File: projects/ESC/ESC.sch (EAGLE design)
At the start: 92 parts, among them J1 1755529, J2 1755529, J3 1755529, J4 1755529, U1 STM32F405RGT6, U10 CSD88584Q5DCT, U11 CSD88584Q5DCT, U12 CSD88584Q5DCT, U13 CSD88584Q5DCT, U2 CSD88584Q5DCT, U3 CSD88584Q5DCT, U4 CSD88584Q5DCT, U5 CSD88584Q5DCT, U6 CSD88584Q5DCT, U7 CSD88584Q5DCT, U8 CSD88584Q5DCT, U9 CSD88584Q5DCT, Y1 ECS-80-S-4X

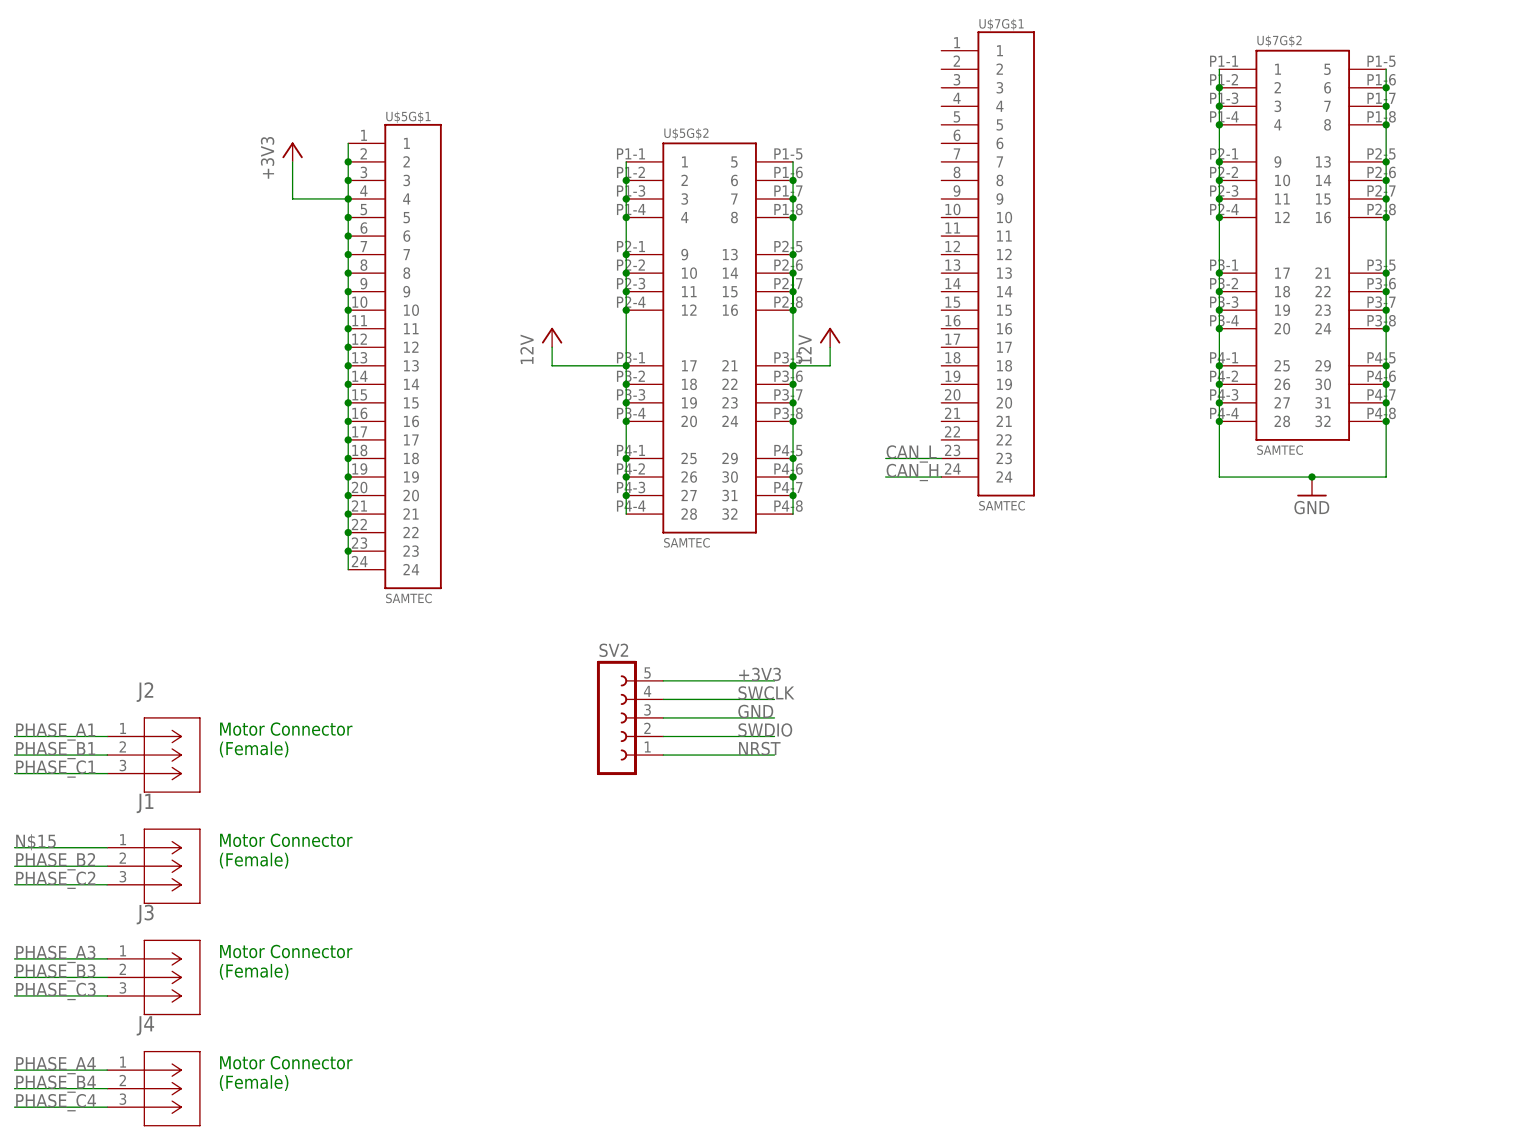
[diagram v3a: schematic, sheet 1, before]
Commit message: made wires thicker
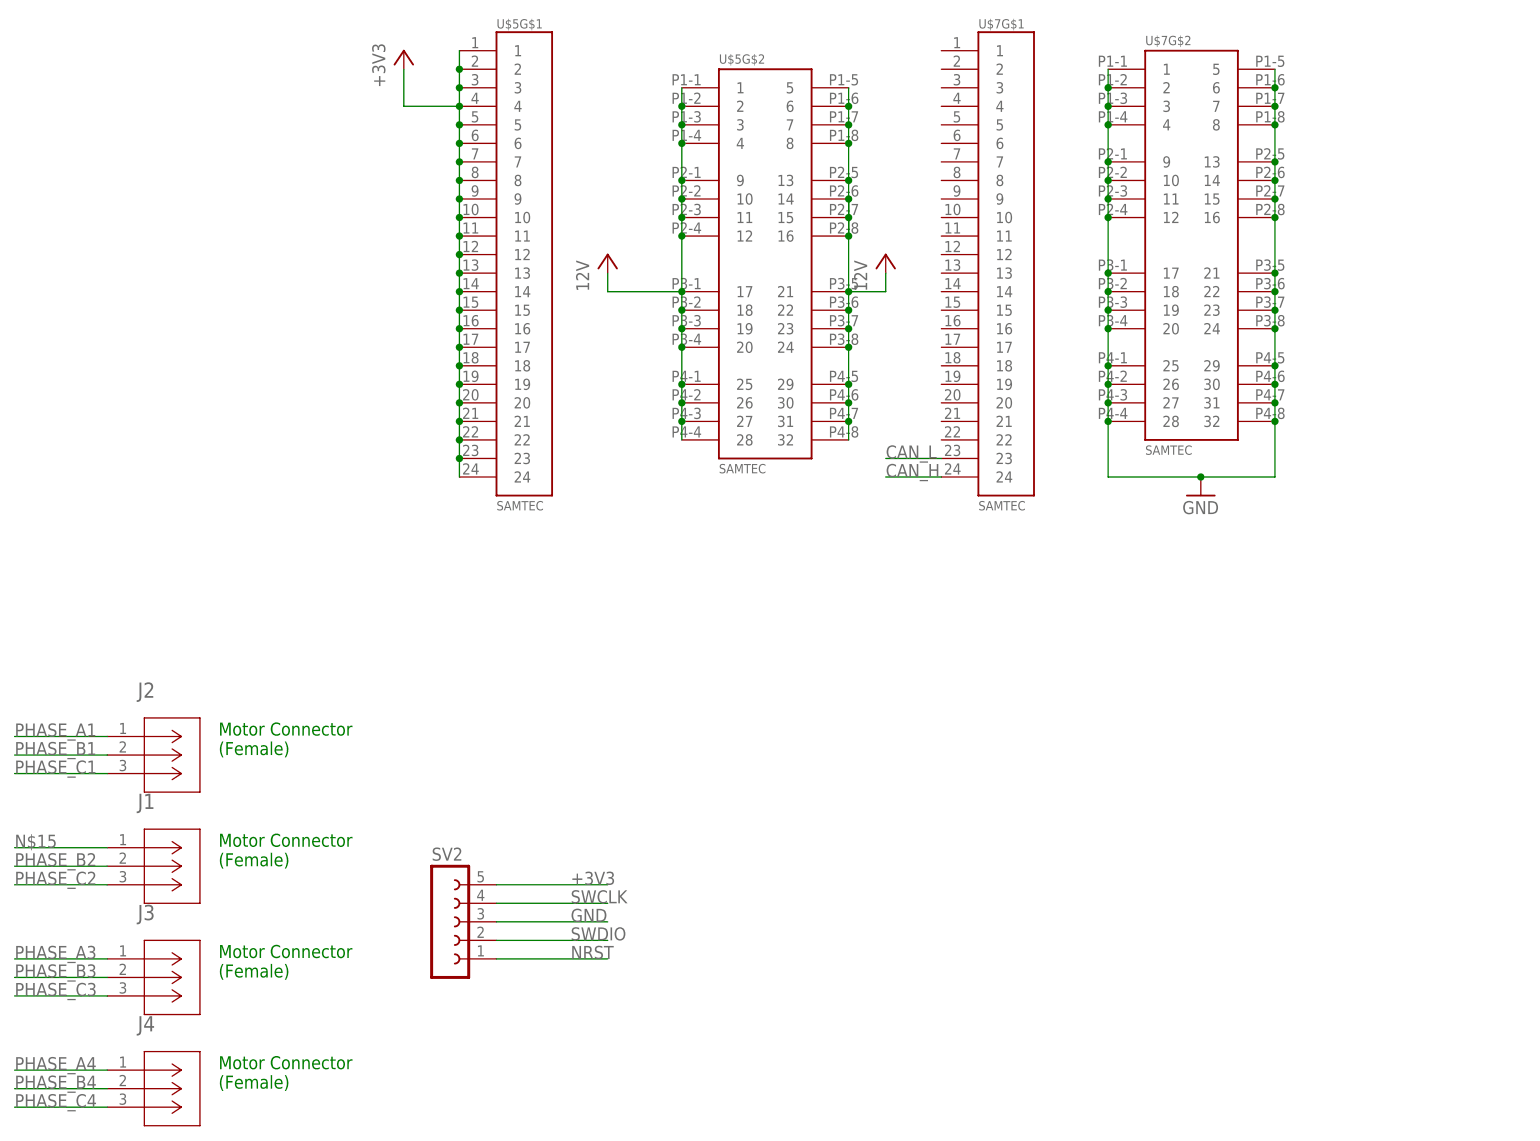
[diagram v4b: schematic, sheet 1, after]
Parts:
- removed SV1: (no value), con-lsta:FE05-1
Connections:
- new net DVDD_2: C23.1, R19.2, R21.2, U$1G$2.DVDD
- net +3V3: no longer SV1.5
- net 12V: no longer C23.1, R10.2, R19.2, R21.2, R8.2, U$1G$2.DVDD
- net DVDD_1: now also R10.2, R8.2
- net GND: no longer SV1.3
- net NRST: no longer SV1.1
- net SWCLK: no longer SV1.4
- net SWDIO: no longer SV1.2
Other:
- moved on the sheet: C10, C12, C16, C32, C33, C34, C35, C38, C39, C4, C40, C41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

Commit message: starting motor 1 (finished motor 2)
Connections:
- net N$15 renamed PHASE_A2
- new net SLC_1B: U4.PGND, U4.PGND_2, U4.PGND_3, U4.PGND_4, U4.PGND_5, U4.PGND_6, U4.PGND_7, U4.PGND_8, U4.PGND_9
- net GHB_1: now also U4.GH; no longer U2.GH
- net GHC_1: now also U2.GH; no longer U4.GH
- net GLB_1: now also U4.GL; no longer U2.GL
- net GLC_1: now also U2.GL; no longer U4.GL
- net PHASE_B1: now also U4.VSW, U4.VSW_2, U4.VSW_3, U4.VSW_4, U4.VSW_5, U4.VSW_6, U4.VSW_7, U4.VSW_8, U4.VSW_9; no longer U2.VSW, U2.VSW_2, U2.VSW_3, U2.VSW_4, U2.VSW_5, U2.VSW_6, U2.VSW_7, U2.VSW_8, U2.VSW_9
- net PHASE_C1: now also U2.VSW, U2.VSW_2, U2.VSW_3, U2.VSW_4, U2.VSW_5, U2.VSW_6, U2.VSW_7, U2.VSW_8, U2.VSW_9; no longer U4.VSW, U4.VSW_2, U4.VSW_3, U4.VSW_4, U4.VSW_5, U4.VSW_6, U4.VSW_7, U4.VSW_8, U4.VSW_9
- net SHB_1: now also U4.SH; no longer U2.SH
- net SHC_1: now also U2.SH; no longer U4.SH
- net SLB_1: no longer U2.PGND, U2.PGND_2, U2.PGND_3, U2.PGND_4, U2.PGND_5, U2.PGND_6, U2.PGND_7, U2.PGND_8, U2.PGND_9
- net SLC_1: now also U2.PGND, U2.PGND_2, U2.PGND_3, U2.PGND_4, U2.PGND_5, U2.PGND_6, U2.PGND_7, U2.PGND_8, U2.PGND_9; no longer U4.PGND, U4.PGND_2, U4.PGND_3, U4.PGND_4, U4.PGND_5, U4.PGND_6, U4.PGND_7, U4.PGND_8, U4.PGND_9
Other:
- moved on the sheet: U2, U4, U5, U7

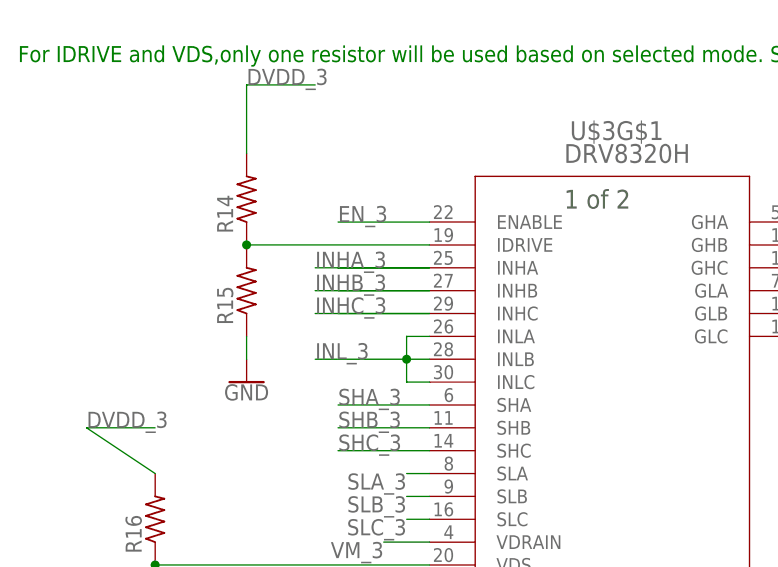
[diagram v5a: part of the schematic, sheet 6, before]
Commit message: finished the left half of the board
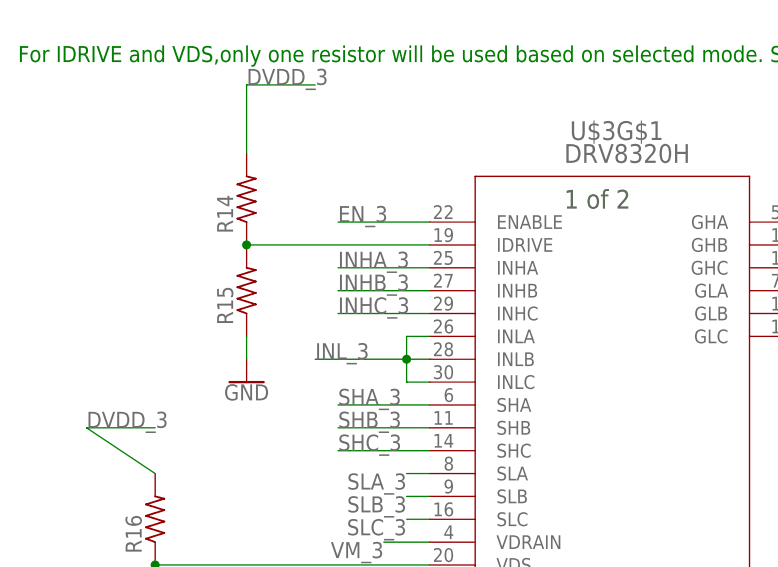
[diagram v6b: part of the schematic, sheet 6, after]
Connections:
- removed net N$10: U$2G$1.INHA
- removed net N$11: U$2G$1.INHB
- removed net N$14: U$2G$1.INHC
- removed net N$20: U$3G$1.INHA
- removed net N$21: U$3G$1.INHB
- removed net N$22: U$3G$1.INHC
- net INHA_1: now also U$2G$1.INHA
- net INHA_3: now also U$3G$1.INHA
- net INHB_1: now also U$2G$1.INHB
- net INHB_3: now also U$3G$1.INHB
- net INHC_1: now also U$2G$1.INHC
- net INHC_3: now also U$3G$1.INHC
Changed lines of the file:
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@@
-</segment>
-</net>
-<net name="N$10" class="0">
-<segment>
-<pinref part="U$2" gate="G$1" pin="INHA"/>
-<wire x1="-68.58" y1="25.4" x2="-78.74" y2="25.4" width="0.1524" layer="91"/>
-</segment>
-</net>
-<net name="N$11" class="0">
-<segment>
-<pinref part="U$2" gate="G$1" pin="INHB"/>
-<wire x1="-68.58" y1="22.86" x2="-78.74" y2="22.86" width="0.1524" layer="91"/>
-</segment>
-</net>
-<net name="N$14" class="0">
-<segment>
-<pinref part="U$2" gate="G$1" pin="INHC"/>
-<wire x1="-68.58" y1="20.32" x2="-78.74" y2="20.32" width="0.1524" layer="91"/>
 </segment>
 </net>
@@
 <net name="INHA_1" class="0">
 <segment>
-<wire x1="-68.58" y1="25.4" x2="-78.74" y2="25.4" width="0.1524" layer="91"/>
-<wire x1="-81.28" y1="25.4" x2="-78.74" y2="25.4" width="0.1524" layer="91"/>
 <label x="-81.28" y="25.4" size="1.778" layer="95"/>
+<pinref part="U$2" gate="G$1" pin="INHA"/>
+<wire x1="-81.28" y1="25.4" x2="-68.58" y2="25.4" width="0.1524" layer="91"/>
 </segment>
 </net>
 <net name="INHB_1" class="0">
 <segment>
-<wire x1="-68.58" y1="22.86" x2="-76.2" y2="22.86" width="0.1524" layer="91"/>
-<wire x1="-81.28" y1="22.86" x2="-76.2" y2="22.86" width="0.1524" layer="91"/>
 <label x="-81.28" y="22.86" size="1.778" layer="95"/>
-</segment>
-</net>
-<net name="INHC_1" class="0">
-<segment>
-<wire x1="-68.58" y1="20.32" x2="-78.74" y2="20.32" width="0.1524" layer="91"/>
-<wire x1="-81.28" y1="20.32" x2="-78.74" y2="20.32" width="0.1524" layer="91"/>
-<label x="-81.28" y="20.32" size="1.778" layer="95"/>
+<pinref part="U$2" gate="G$1" pin="INHB"/>
+<wire x1="-68.58" y1="22.86" x2="-81.28" y2="22.86" width="0.1524" layer="91"/>
 </segment>
 </net>
@@
 <wire x1="-68.58" y1="-7.62" x2="-99.06" y2="-7.62" width="0.1524" layer="91"/>
 <junction x="-99.06" y="-7.62"/>
+</segment>
+</net>
+<net name="INHC_1" class="0">
+<segment>
+<pinref part="U$2" gate="G$1" pin="INHC"/>
+<wire x1="-68.58" y1="20.32" x2="-81.28" y2="20.32" width="0.1524" layer="91"/>
+<label x="-81.28" y="20.32" size="1.778" layer="95"/>
 </segment>
 </net>
@@
 </busses>
 <nets>
-<net name="N$20" class="0">
-<segment>
-<pinref part="U$3" gate="G$1" pin="INHA"/>
-<wire x1="-58.42" y1="17.78" x2="-68.58" y2="17.78" width="0.1524" layer="91"/>
-</segment>
-</net>
-<net name="N$21" class="0">
-<segment>
-<pinref part="U$3" gate="G$1" pin="INHB"/>
-<wire x1="-58.42" y1="15.24" x2="-68.58" y2="15.24" width="0.1524" layer="91"/>
-</segment>
-</net>
-<net name="N$22" class="0">
-<segment>
-<pinref part="U$3" gate="G$1" pin="INHC"/>
-<wire x1="-58.42" y1="12.7" x2="-68.58" y2="12.7" width="0.1524" layer="91"/>
-</segment>
-</net>
 <net name="DVDD_3" class="0">
 <segment>
@@
 </segment>
 </net>
-<net name="INHA_3" class="0">
-<segment>
-<wire x1="-58.42" y1="17.78" x2="-68.58" y2="17.78" width="0.1524" layer="91"/>
-<wire x1="-71.12" y1="17.78" x2="-68.58" y2="17.78" width="0.1524" layer="91"/>
-<label x="-71.12" y="17.78" size="1.778" layer="95"/>
-</segment>
-</net>
-<net name="INHB_3" class="0">
-<segment>
-<wire x1="-58.42" y1="15.24" x2="-66.04" y2="15.24" width="0.1524" layer="91"/>
-<wire x1="-71.12" y1="15.24" x2="-66.04" y2="15.24" width="0.1524" layer="91"/>
-<label x="-71.12" y="15.24" size="1.778" layer="95"/>
-</segment>
-</net>
-<net name="INHC_3" class="0">
-<segment>
-<wire x1="-58.42" y1="12.7" x2="-68.58" y2="12.7" width="0.1524" layer="91"/>
-<wire x1="-71.12" y1="12.7" x2="-68.58" y2="12.7" width="0.1524" layer="91"/>
-<label x="-71.12" y="12.7" size="1.778" layer="95"/>
-</segment>
-</net>
 <net name="INL_3" class="0">
 <segment>
@@
 </segment>
 </net>
+<net name="INHA_3" class="0">
+<segment>
+<pinref part="U$3" gate="G$1" pin="INHA"/>
+<wire x1="-58.42" y1="17.78" x2="-68.58" y2="17.78" width="0.1524" layer="91"/>
+<label x="-68.58" y="17.78" size="1.778" layer="95"/>
+</segment>
+</net>
+<net name="INHB_3" class="0">
+<segment>
+<pinref part="U$3" gate="G$1" pin="INHB"/>
+<wire x1="-58.42" y1="15.24" x2="-68.58" y2="15.24" width="0.1524" layer="91"/>
+<label x="-68.58" y="15.24" size="1.778" layer="95"/>
+</segment>
+</net>
+<net name="INHC_3" class="0">
+<segment>
+<pinref part="U$3" gate="G$1" pin="INHC"/>
+<wire x1="-58.42" y1="12.7" x2="-68.58" y2="12.7" width="0.1524" layer="91"/>
+<label x="-68.58" y="12.7" size="1.778" layer="95"/>
+</segment>
+</net>

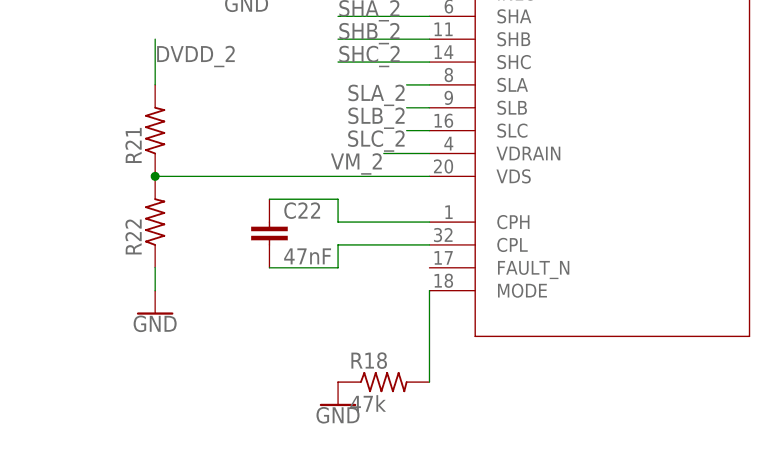
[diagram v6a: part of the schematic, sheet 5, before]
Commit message: Added Fault connection from drvs to stm
forgot to do this earlier
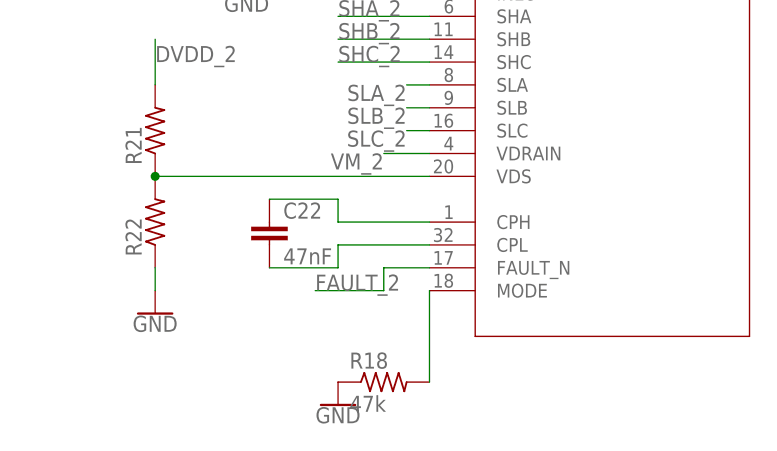
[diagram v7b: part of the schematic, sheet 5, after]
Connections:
- net FAULT_1: now also U$2G$1.FAULT_N
- net FAULT_2: now also U$1G$1.FAULT_N
- net FAULT_3: now also U$3G$1.FAULT_N
- net FAULT_4: now also U$4G$1.FAULT_N
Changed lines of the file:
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@@
 <?xml version="1.0" encoding="utf-8"?>
 <!DOCTYPE eagle SYSTEM "eagle.dtd">
-<eagle version="9.4.1">
+<eagle version="9.5.1">
 <drawing>
 <settings>
@@
 </segment>
 </net>
+<net name="FAULT_1" class="0">
+<segment>
+<pinref part="U$2" gate="G$1" pin="FAULT_N"/>
+<wire x1="-68.58" y1="-17.78" x2="-76.2" y2="-17.78" width="0.1524" layer="91"/>
+<label x="-76.2" y="-17.78" size="1.778" layer="95"/>
+</segment>
+</net>
 </nets>
 </sheet>
@@
 </segment>
 </net>
+<net name="FAULT_2" class="0">
+<segment>
+<pinref part="U$1" gate="G$1" pin="FAULT_N"/>
+<wire x1="71.12" y1="60.96" x2="66.04" y2="60.96" width="0.1524" layer="91"/>
+<wire x1="66.04" y1="60.96" x2="66.04" y2="58.42" width="0.1524" layer="91"/>
+<wire x1="66.04" y1="58.42" x2="58.42" y2="58.42" width="0.1524" layer="91"/>
+<label x="58.42" y="58.42" size="1.778" layer="95"/>
+</segment>
+</net>
 </nets>
 </sheet>
@@
 </segment>
 </net>
+<net name="FAULT_3" class="0">
+<segment>
+<pinref part="U$3" gate="G$1" pin="FAULT_N"/>
+<wire x1="-58.42" y1="-25.4" x2="-63.5" y2="-25.4" width="0.1524" layer="91"/>
+<wire x1="-63.5" y1="-25.4" x2="-63.5" y2="-27.94" width="0.1524" layer="91"/>
+<wire x1="-63.5" y1="-27.94" x2="-71.12" y2="-27.94" width="0.1524" layer="91"/>
+<label x="-71.12" y="-27.94" size="1.778" layer="95"/>
+</segment>
+</net>
 </nets>
 </sheet>
@@
 </segment>
 </net>
+<net name="FAULT_4" class="0">
+<segment>
+<pinref part="U$4" gate="G$1" pin="FAULT_N"/>
+<wire x1="-58.42" y1="-25.4" x2="-63.5" y2="-25.4" width="0.1524" layer="91"/>
+<wire x1="-63.5" y1="-25.4" x2="-63.5" y2="-27.94" width="0.1524" layer="91"/>
+<wire x1="-63.5" y1="-27.94" x2="-71.12" y2="-27.94" width="0.1524" layer="91"/>
+<label x="-71.12" y="-27.94" size="1.778" layer="95"/>
+</segment>
+</net>

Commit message: ERC stuff 1
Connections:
- removed net N$37: U$4G$1.INHA
- removed net N$38: U$4G$1.INHB
- removed net N$39: U$4G$1.INHC
- removed net SLC_1B: U4.PGND, U4.PGND_2, U4.PGND_3, U4.PGND_4, U4.PGND_5, U4.PGND_6, U4.PGND_7, U4.PGND_8, U4.PGND_9
- net INHA_4: now also U$4G$1.INHA
- net INHB_4: now also U$4G$1.INHB
- net INHC_2: now also U$1G$1.INHC
- net INHC_3: no longer U$1G$1.INHC
- net INHC_4: now also U$4G$1.INHC
- net SLB_1: now also U4.PGND, U4.PGND_2, U4.PGND_3, U4.PGND_4, U4.PGND_5, U4.PGND_6, U4.PGND_7, U4.PGND_8, U4.PGND_9
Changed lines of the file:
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@@
 <junction x="66.04" y="25.4"/>
 <pinref part="GND8" gate="1" pin="GND"/>
+<junction x="78.74" y="25.4"/>
 </segment>
 <segment>
@@
 <junction x="205.74" y="104.14"/>
 <pinref part="GND16" gate="1" pin="GND"/>
+<junction x="218.44" y="104.14"/>
 </segment>
 <segment>
@@
 </segment>
 </net>
-<net name="INHC_3" class="0">
-<segment>
-<pinref part="U$1" gate="G$1" pin="INHC"/>
-<wire x1="71.12" y1="99.06" x2="58.42" y2="99.06" width="0.1524" layer="91"/>
-<label x="58.42" y="99.06" size="1.778" layer="95"/>
-</segment>
-</net>
 <net name="DVDD_2" class="0">
 <segment>
@@
 <wire x1="66.04" y1="58.42" x2="58.42" y2="58.42" width="0.1524" layer="91"/>
 <label x="58.42" y="58.42" size="1.778" layer="95"/>
+</segment>
+</net>
+<net name="INHC_2" class="0">
+<segment>
+<pinref part="U$1" gate="G$1" pin="INHC"/>
+<wire x1="71.12" y1="99.06" x2="58.42" y2="99.06" width="0.1524" layer="91"/>
+<label x="58.42" y="99.06" size="1.778" layer="95"/>
 </segment>
 </net>
@@
 <junction x="76.2" y="17.78"/>
 <pinref part="GND12" gate="1" pin="GND"/>
+<junction x="88.9" y="17.78"/>
 </segment>
 <segment>
@@
 </busses>
 <nets>
-<net name="N$37" class="0">
+<net name="INHA_4" class="0">
 <segment>
 <pinref part="U$4" gate="G$1" pin="INHA"/>
-<wire x1="-58.42" y1="17.78" x2="-68.58" y2="17.78" width="0.1524" layer="91"/>
-</segment>
-</net>
-<net name="N$38" class="0">
-<segment>
-<pinref part="U$4" gate="G$1" pin="INHB"/>
-<wire x1="-58.42" y1="15.24" x2="-68.58" y2="15.24" width="0.1524" layer="91"/>
-</segment>
-</net>
-<net name="N$39" class="0">
-<segment>
-<pinref part="U$4" gate="G$1" pin="INHC"/>
-<wire x1="-58.42" y1="12.7" x2="-68.58" y2="12.7" width="0.1524" layer="91"/>
+<wire x1="-58.42" y1="17.78" x2="-71.12" y2="17.78" width="0.1524" layer="91"/>
+<label x="-71.12" y="17.78" size="1.778" layer="95"/>
 </segment>
 </net>
@@
 <junction x="76.2" y="17.78"/>
 <pinref part="GND20" gate="1" pin="GND"/>
+<junction x="88.9" y="17.78"/>
 </segment>
 <segment>
@@
 </segment>
 </net>
-<net name="INHA_4" class="0">
-<segment>
-<wire x1="-58.42" y1="17.78" x2="-68.58" y2="17.78" width="0.1524" layer="91"/>
-<wire x1="-71.12" y1="17.78" x2="-68.58" y2="17.78" width="0.1524" layer="91"/>
-<label x="-71.12" y="17.78" size="1.778" layer="95"/>
-</segment>
-</net>
 <net name="INHB_4" class="0">
 <segment>
-<wire x1="-58.42" y1="15.24" x2="-66.04" y2="15.24" width="0.1524" layer="91"/>
-<wire x1="-71.12" y1="15.24" x2="-66.04" y2="15.24" width="0.1524" layer="91"/>
+<wire x1="-71.12" y1="15.24" x2="-58.42" y2="15.24" width="0.1524" layer="91"/>
 <label x="-71.12" y="15.24" size="1.778" layer="95"/>
+<pinref part="U$4" gate="G$1" pin="INHB"/>
 </segment>
 </net>
 <net name="INHC_4" class="0">
 <segment>
-<wire x1="-58.42" y1="12.7" x2="-68.58" y2="12.7" width="0.1524" layer="91"/>
-<wire x1="-71.12" y1="12.7" x2="-68.58" y2="12.7" width="0.1524" layer="91"/>
+<wire x1="-58.42" y1="12.7" x2="-71.12" y2="12.7" width="0.1524" layer="91"/>
 <label x="-71.12" y="12.7" size="1.778" layer="95"/>
+<pinref part="U$4" gate="G$1" pin="INHC"/>
 </segment>
 </net>
@@
 </segment>
 </net>
-<net name="SLC_1B" class="0">
+<net name="SLB_1" class="0">
 <segment>
 <pinref part="U4" gate="A" pin="PGND_2"/>
